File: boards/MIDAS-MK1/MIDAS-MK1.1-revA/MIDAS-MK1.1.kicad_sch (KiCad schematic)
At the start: 106 parts, among them J101 Left, J102 Right, J103 Conn_01x02, J105 Conn_01x02, J106 USB4105-GF-A, J107 DM3BT-DSF-PEJS, J108 Conn_01x02, J110 2157601003, J111 2157601003, SW101 SW_Push, SW102 SW_Push, U101 TCAL9539-Q1, U102 TCAL9539-Q1, U103 TCAL9539-Q1, U104 ESP32-S3-WROOM-1U, U105 MCP2518FDT-xSL, U106 MTFCxxxx, U107 TCAN337G, U108 ADS7138-Q1, U109 ECMF02-2AMX6, Y101 40MHz

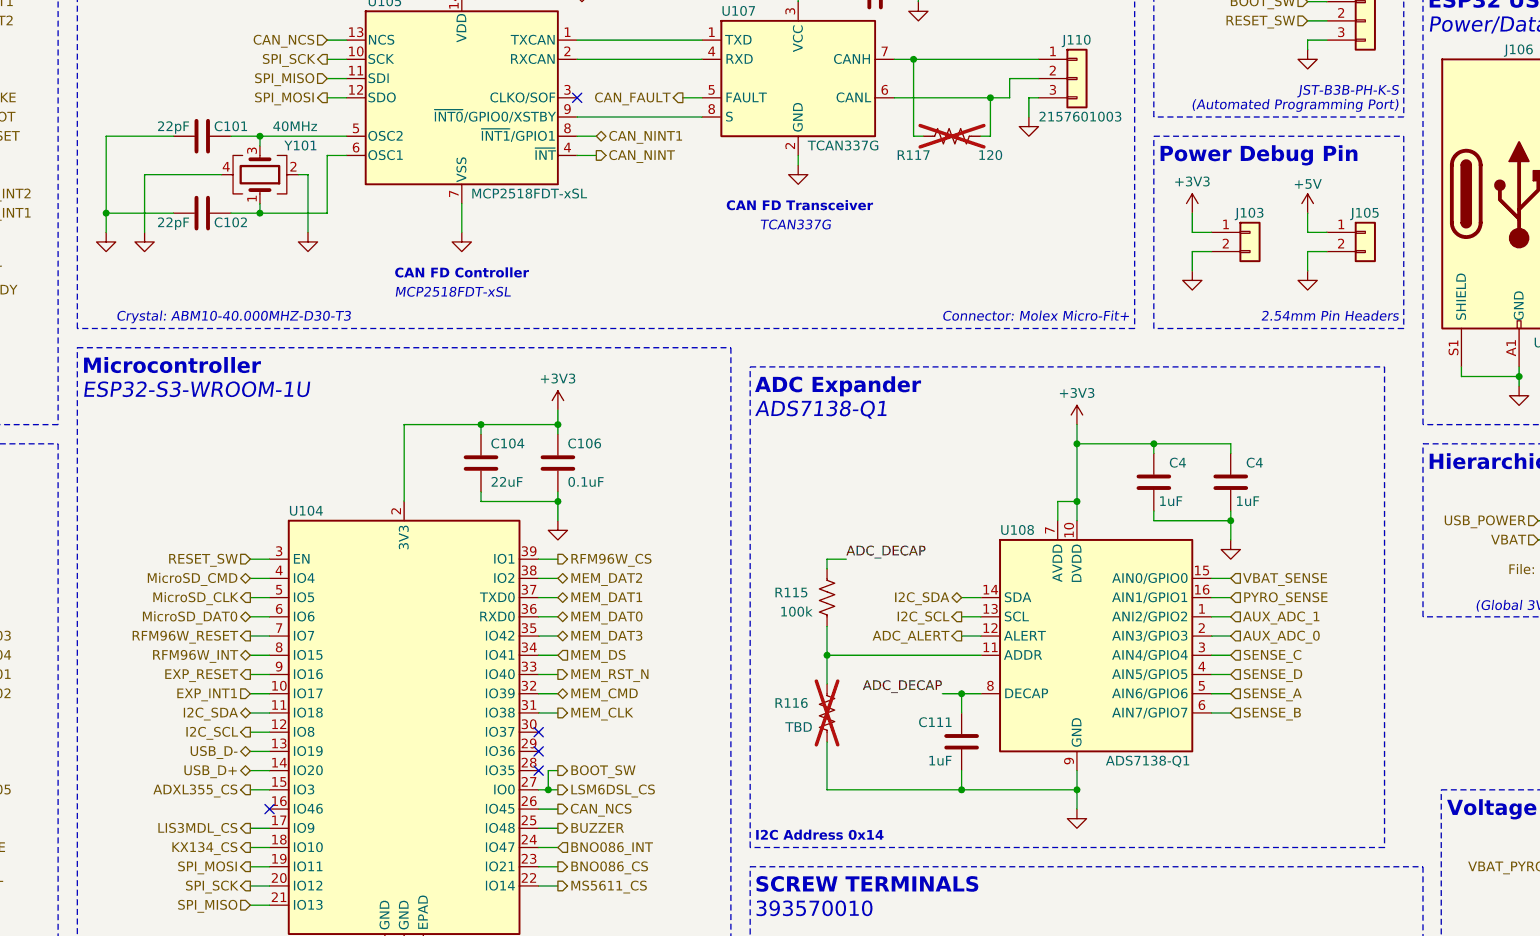
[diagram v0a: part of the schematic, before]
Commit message: switched LSM CS for ADXL CS on MCU and made small adjustments
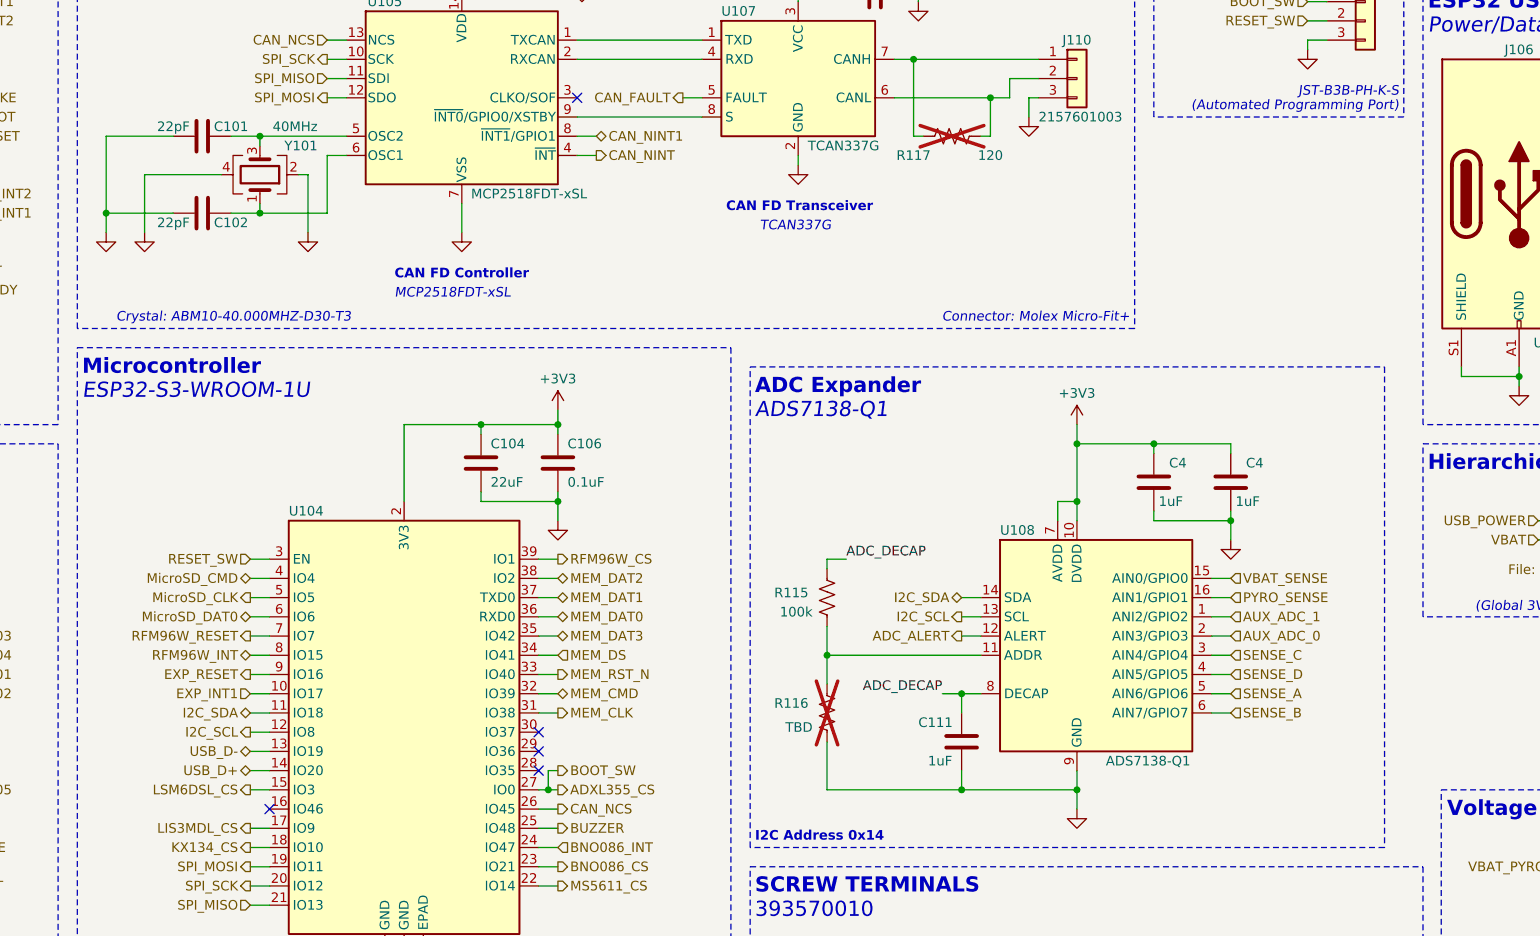
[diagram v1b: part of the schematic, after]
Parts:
- removed J103, J105: Conn_01x02, Connector_PinSocket_2.54mm:PinSocket_1x02_P2.54mm_Vertical, symbol Connector_Generic:Conn_01x02
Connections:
- net BOOT_SW is gone; now on net ADXL355_CS: C103.2, J104.1 (Pin_1), SW101.2, U104.27 (IO0)
- net ADXL355_CS: no longer U104.15 (IO3)
- new net LSM6DSL_CS: U104.15 (IO3)
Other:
- note removed: "Power Debug Pin"
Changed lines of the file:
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@@
     (stroke (width 0) (type default))
   )
-  (wire (pts (xy 236.22 144.78) (xy 233.68 144.78))
-    (stroke (width 0) (type default))
-  )
   (wire (pts (xy 342.9 133.35) (xy 342.9 134.62))
     (stroke (width 0) (type default))
@@
     (stroke (width 0) (type default))
   )
-  (wire (pts (xy 248.92 142.24) (xy 248.92 144.78))
-    (stroke (width 0) (type default))
-  )
   (wire (pts (xy 203.2 205.74) (xy 203.2 208.28))
     (stroke (width 0) (type default))
@@
     (stroke (width 0) (type default))
   )
-  (wire (pts (xy 248.92 147.32) (xy 251.46 147.32))
-    (stroke (width 0) (type default))
-  )
   (wire (pts (xy 317.5 22.86) (xy 320.04 22.86))
     (stroke (width 0) (type default))
@@
     (stroke (width 0) (type default))
   )
-  (wire (pts (xy 248.92 149.86) (xy 248.92 147.32))
-    (stroke (width 0) (type default))
-  )
   (wire (pts (xy 284.48 256.54) (xy 281.94 256.54))
     (stroke (width 0) (type default))
@@
     (stroke (width 0) (type default))
   )
-  (wire (pts (xy 233.68 147.32) (xy 236.22 147.32))
-    (stroke (width 0) (type default))
-  )
   (wire (pts (xy 378.46 200.66) (xy 381 200.66))
     (stroke (width 0) (type default))
@@
     (stroke (width 0) (type default))
   )
-  (wire (pts (xy 233.68 144.78) (xy 233.68 142.24))
-    (stroke (width 0) (type default))
-  )
   (wire (pts (xy 389.89 92.71) (xy 389.89 91.44))
     (stroke (width 0) (type default))
@@
     (stroke (width 0) (type default))
   )
-  (wire (pts (xy 248.92 144.78) (xy 251.46 144.78))
-    (stroke (width 0) (type default))
-  )
   (wire (pts (xy 60.96 43.18) (xy 63.5 43.18))
     (stroke (width 0) (type default))
@@
     (stroke (width 0) (type default))
   )
-  (wire (pts (xy 233.68 149.86) (xy 233.68 147.32))
-    (stroke (width 0) (type default))
-  )
   (wire (pts (xy 30.48 200.66) (xy 33.02 200.66))
     (stroke (width 0) (type default))
@@
     (fill (type none))
   )
-  (rectangle (start 228.6 132.08) (end 261.62 157.48)
-    (stroke (width 0) (type dash))
-    (fill (type none))
-  )
   (rectangle (start 266.573 218.44) (end 294.64 281.94)
     (stroke (width 0) (type dash))
@@
     (effects (font (size 1.27 1.27) italic) (justify left bottom))
   )
-  (text "Power Debug Pin\n\n" (at 229.235 139.065 0)
-    (effects (font (size 2 2) (thickness 0.4) bold) (justify left bottom))
-  )
   (text "393570010" (at 175.895 235.585 0)
     (effects (font (size 2 2)) (justify left bottom))
@@
     (effects (font (size 1.27 1.27)) (justify left bottom))
   )
-  (text "2.54mm Pin Headers" (at 260.985 156.845 0)
-    (effects (font (size 1.27 1.27) italic) (justify right bottom))
-  )
   (text "ESP32 Boot Button" (at 99.695 260.35 0)
     (effects (font (size 2 2) (thickness 0.4) bold) (justify left bottom))
@@
     (effects (font (size 1.27 1.27)) (justify right))
   )
-  (hierarchical_label "ADXL355_CS" (shape output) (at 109.22 218.44 180) (fields_autoplaced)
-    (effects (font (size 1.27 1.27)) (justify right))
+  (hierarchical_label "ADXL355_CS" (shape output) (at 149.86 218.44 0) (fields_autoplaced)
+    (effects (font (size 1.27 1.27)) (justify left))
   )
   (hierarchical_label "FIRE_A" (shape output) (at 63.5 73.66 0) (fields_autoplaced)
@@
     (effects (font (size 1.27 1.27)) (justify right))
   )
-  (hierarchical_label "LSM6DSL_CS" (shape output) (at 149.86 218.44 0) (fields_autoplaced)
-    (effects (font (size 1.27 1.27)) (justify left))
-  )
   (hierarchical_label "MEM_DAT3" (shape bidirectional) (at 149.86 198.12 0) (fields_autoplaced)
     (effects (font (size 1.27 1.27)) (justify left))
@@
     (effects (font (size 1.27 1.27)) (justify right))
   )
+  (hierarchical_label "LSM6DSL_CS" (shape output) (at 109.22 218.44 180) (fields_autoplaced)
+    (effects (font (size 1.27 1.27)) (justify right))
+  )
   (hierarchical_label "VBAT" (shape output) (at 247.523 241.3 0) (fields_autoplaced)
     (effects (font (size 1.27 1.27)) (justify left))
@@
     )
   )
-  (symbol (lib_id "power:GND") (at 248.92 149.86 0) (unit 1)
-    (in_bom yes) (on_board yes) (dnp no) (fields_autoplaced)
-    (property "Reference" "#PWR0139" (at 248.92 156.21 0)
-      (effects (font (size 1.27 1.27)) hide)
-    )
-    (property "Value" "GND" (at 248.92 154.305 0)
-      (effects (font (size 1.27 1.27)) hide)
-    )
-    (property "Footprint" "" (at 248.92 149.86 0)
-      (effects (font (size 1.27 1.27)) hide)
-    )
-    (property "Datasheet" "" (at 248.92 149.86 0)
-      (effects (font (size 1.27 1.27)) hide)
-    )
-    (pin "1")
-    (instances
-      (project "MIDAS-MK1.1"
-        (path "/6007cf46-4651-4a02-8f98-d5846f3575c7"
-          (reference "#PWR0139") (unit 1)
-        )
-      )
-    )
-  )
   (symbol (lib_id "Device:C") (at 149.86 175.26 0) (unit 1)
     (in_bom yes) (on_board yes) (dnp no)
@@
     )
   )
-  (symbol (lib_id "power:+5V") (at 248.92 142.24 0) (unit 1)
-    (in_bom yes) (on_board yes) (dnp no)
-    (property "Reference" "#PWR0138" (at 248.92 146.05 0)
-      (effects (font (size 1.27 1.27)) hide)
-    )
-    (property "Value" "+5V" (at 248.92 138.43 0)
-      (effects (font (size 1.27 1.27)))
-    )
-    (property "Footprint" "" (at 248.92 142.24 0)
-      (effects (font (size 1.27 1.27)) hide)
-    )
-    (property "Datasheet" "" (at 248.92 142.24 0)
-      (effects (font (size 1.27 1.27)) hide)
-    )
-    (pin "1")
-    (instances
-      (project "MIDAS-MK1.1"
-        (path "/6007cf46-4651-4a02-8f98-d5846f3575c7"
-          (reference "#PWR0138") (unit 1)
-        )
-      )
-    )
-  )
   (symbol (lib_id "Device:C") (at 203.2 212.09 0) (unit 1)
     (in_bom yes) (on_board yes) (dnp no)
@@
     )
   )
-  (symbol (lib_id "power:+3V3") (at 233.68 142.24 0) (unit 1)
-    (in_bom yes) (on_board yes) (dnp no) (fields_autoplaced)
-    (property "Reference" "#PWR0133" (at 233.68 146.05 0)
-      (effects (font (size 1.27 1.27)) hide)
-    )
-    (property "Value" "+3V3" (at 233.68 138.1069 0)
-      (effects (font (size 1.27 1.27)))
-    )
-    (property "Footprint" "" (at 233.68 142.24 0)
-      (effects (font (size 1.27 1.27)) hide)
-    )
-    (property "Datasheet" "" (at 233.68 142.24 0)
-      (effects (font (size 1.27 1.27)) hide)
-    )
-    (pin "1")
-    (instances
-      (project "MIDAS-MK1.1"
-        (path "/6007cf46-4651-4a02-8f98-d5846f3575c7"
-          (reference "#PWR0133") (unit 1)
-        )
-      )
-    )
-  )
   (symbol (lib_id "power:GND") (at 307.34 152.4 0) (unit 1)
     (in_bom yes) (on_board yes) (dnp no)
@@
     )
   )
-  (symbol (lib_id "Connector_Generic:Conn_01x02") (at 256.54 144.78 0) (unit 1)
-    (in_bom yes) (on_board yes) (dnp no)
-    (property "Reference" "J105" (at 256.54 142.24 0)
-      (effects (font (size 1.27 1.27)))
-    )
-    (property "Value" "Conn_01x02" (at 256.54 149.86 0)
-      (effects (font (size 1.27 1.27)) hide)
-    )
-    (property "Footprint" "Connector_PinSocket_2.54mm:PinSocket_1x02_P2.54mm_Vertical" (at 256.54 144.78 0)
-      (effects (font (size 1.27 1.27)) hide)
-    )
-    (property "Datasheet" "~" (at 256.54 144.78 0)
-      (effects (font (size 1.27 1.27)) hide)
-    )
-    (pin "1")
-    (pin "2")
-    (instances
-      (project "MIDAS-MK1.1"
-        (path "/6007cf46-4651-4a02-8f98-d5846f3575c7"
-          (reference "J105") (unit 1)
-        )
-      )
-    )
-  )
   (symbol (lib_id "Device:R_US") (at 101.6 33.02 180) (unit 1)
     (in_bom yes) (on_board yes) (dnp no)
@@
     )
   )
-  (symbol (lib_id "Connector_Generic:Conn_01x02") (at 241.3 144.78 0) (unit 1)
-    (in_bom yes) (on_board yes) (dnp no)
-    (property "Reference" "J103" (at 241.3 142.24 0)
-      (effects (font (size 1.27 1.27)))
-    )
-    (property "Value" "Conn_01x02" (at 241.3 149.86 0)
-      (effects (font (size 1.27 1.27)) hide)
-    )
-    (property "Footprint" "Connector_PinSocket_2.54mm:PinSocket_1x02_P2.54mm_Vertical" (at 241.3 144.78 0)
-      (effects (font (size 1.27 1.27)) hide)
-    )
-    (property "Datasheet" "~" (at 241.3 144.78 0)
-      (effects (font (size 1.27 1.27)) hide)
-    )
-    (pin "1")
-    (pin "2")
-    (instances
-      (project "MIDAS-MK1.1"
-        (path "/6007cf46-4651-4a02-8f98-d5846f3575c7"
-          (reference "J103") (unit 1)
-        )
-      )
-    )
-  )
   (symbol (lib_id "Device:R_US") (at 320.04 132.08 90) (unit 1)
     (in_bom yes) (on_board yes) (dnp no)
@@
         )
       )
-    )
-  )
-  (symbol (lib_id "power:GND") (at 233.68 149.86 0) (unit 1)
-    (in_bom yes) (on_board yes) (dnp no) (fields_autoplaced)
-    (property "Reference" "#PWR0134" (at 233.68 156.21 0)
-      (effects (font (size 1.27 1.27)) hide)
-    )
-    (property "Value" "GND" (at 233.68 154.305 0)
-      (effects (font (size 1.27 1.27)) hide)
-    )
-    (property "Footprint" "" (at 233.68 149.86 0)
-      (effects (font (size 1.27 1.27)) hide)
-    )
-    (property "Datasheet" "" (at 233.68 149.86 0)
-      (effects (font (size 1.27 1.27)) hide)
-    )
-    (pin "1")
-    (instances
-      (project "MIDAS-MK1.1"
-        (path "/6007cf46-4651-4a02-8f98-d5846f3575c7"
-          (reference "#PWR0134") (unit 1)
-        )
-      )

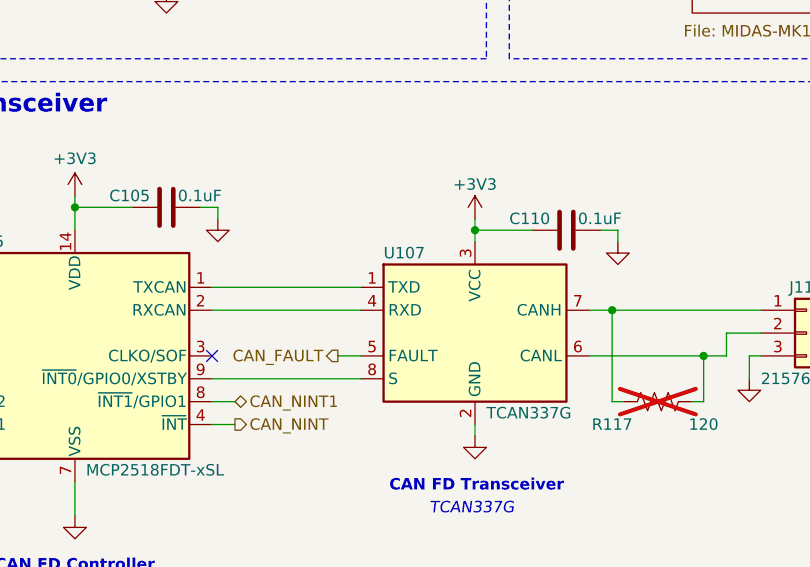
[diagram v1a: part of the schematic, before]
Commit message: added CAN_FAULT pullup
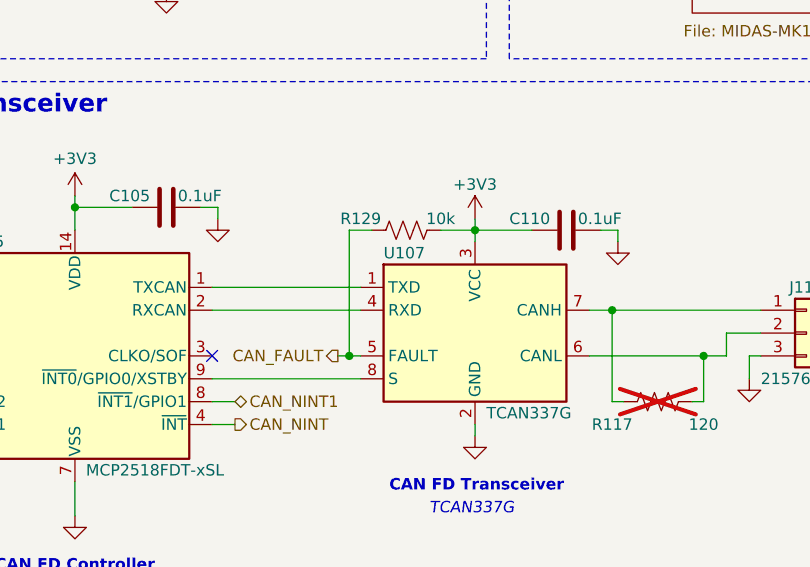
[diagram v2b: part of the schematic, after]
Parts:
- added R129: 10k, Resistor_SMD:R_0603_1608Metric, symbol Device:R_US
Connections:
- net +3V3: now also R129.1
- net CAN_FAULT: now also R129.2
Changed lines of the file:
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@@
   (junction (at 358.14 213.36) (diameter 0) (color 0 0 0 0)
   )
+  (junction (at 167.64 127) (diameter 0) (color 0 0 0 0)
+  )
   (junction (at 41.91 259.08) (diameter 0) (color 0 0 0 0)
   )
@@
     (stroke (width 0) (type default))
   )
+  (wire (pts (xy 177.8 113.03) (xy 181.61 113.03))
+    (stroke (width 0) (type default))
+  )
   (wire (pts (xy 203.2 205.74) (xy 203.2 208.28))
     (stroke (width 0) (type default))
@@
     (stroke (width 0) (type default))
   )
+  (wire (pts (xy 167.64 127) (xy 168.91 127))
+    (stroke (width 0) (type default))
+  )
   (wire (pts (xy 196.85 132.08) (xy 198.12 132.08))
     (stroke (width 0) (type default))
@@
     (stroke (width 0) (type default))
   )
+  (wire (pts (xy 167.64 113.03) (xy 170.18 113.03))
+    (stroke (width 0) (type default))
+  )
   (wire (pts (xy 396.24 72.39) (xy 396.24 73.66))
     (stroke (width 0) (type default))
@@
     (stroke (width 0) (type default))
   )
+  (wire (pts (xy 167.64 127) (xy 167.64 113.03))
+    (stroke (width 0) (type default))
+  )
   (wire (pts (xy 33.02 113.03) (xy 33.02 121.92))
     (stroke (width 0) (type default))
@@
     (stroke (width 0) (type default))
   )
-  (wire (pts (xy 166.37 127) (xy 168.91 127))
+  (wire (pts (xy 166.37 127) (xy 167.64 127))
     (stroke (width 0) (type default))
   )
@@
         )
       )
+    )
+  )
+  (symbol (lib_id "Device:R_US") (at 173.99 113.03 270) (unit 1)
+    (in_bom yes) (on_board yes) (dnp no)
+    (property "Reference" "R129" (at 168.91 111.76 90)
+      (effects (font (size 1.27 1.27)))
+    )
+    (property "Value" "10k" (at 177.8 111.76 90)
+      (effects (font (size 1.27 1.27)))
+    )
+    (property "Footprint" "Resistor_SMD:R_0603_1608Metric" (at 173.736 114.046 90)
+      (effects (font (size 1.27 1.27)) hide)
+    )
+    (property "Datasheet" "~" (at 173.99 113.03 0)
+      (effects (font (size 1.27 1.27)) hide)
+    )
+    (pin "1")
+    (pin "2")
+    (instances
+      (project "MIDAS-MK1.1"
+        (path "/6007cf46-4651-4a02-8f98-d5846f3575c7"
+          (reference "R129") (unit 1)
+        )
+      )
+      (project "TARS-MK4.1-TELEM"
+        (path "/e63e39d7-6ac0-4ffd-8aa3-1841a4541b55"
+          (reference "R123") (unit 1)
+        )
+      )
